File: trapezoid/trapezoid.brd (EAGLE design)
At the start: 90 x 35 mm, 29 parts, among them IC2 LGD20H, U1 MMA8452Q, U2 microSD, U3 DS3234, U4 MCP73831

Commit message: postiotedn arduino pins on board
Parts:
- moved J2 3.29 mm to (72.9, 29.9)
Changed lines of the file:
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@@
 <element name="IC2" library="microbuilder" package="L3GD20H_LGA16L" value="LGD20H" x="-49.53" y="25.4"/>
 <element name="J1" library="SparkFun-Connectors" package="1X12" value="" x="88.17" y="2.01" rot="R90"/>
-<element name="J2" library="SparkFun-Connectors" package="1X12" value="" x="76.18" y="30.45" rot="R270"/>
+<element name="J2" library="SparkFun-Connectors" package="1X12" value="" x="72.93" y="29.95" rot="R270"/>
 <element name="J3" library="SparkFun-Connectors" package="1X02_LOCK" value="" x="-49.53" y="43.18"/>
 <element name="JP1" library="SparkFun-Connectors" package="JST-2-SMD@1" value="JST" x="-43.18" y="29.21">
@@
 <wire x1="-47.31" y1="54.61" x2="-42.86" y2="54.61" width="0" layer="19" extent="1-1"/>
 <wire x1="-47.31" y1="48.26" x2="-41.26" y2="49.53" width="0" layer="19" extent="1-1"/>
-<wire x1="76.18" y1="27.91" x2="-41.26" y2="49.53" width="0" layer="19" extent="1-1"/>
+<wire x1="72.93" y1="27.41" x2="-41.26" y2="49.53" width="0" layer="19" extent="1-1"/>
 <wire x1="-13.965" y1="38.6" x2="-15.24" y2="48.2299" width="0" layer="19" extent="1-1"/>
 <wire x1="-13.965" y1="37.6" x2="-13.965" y2="38.6" width="0" layer="19" extent="1-1"/>
@@
 <contactref element="U2" pad="2"/>
 <contactref element="J2" pad="12"/>
-<wire x1="-21.81" y1="11.57" x2="76.18" y2="2.51" width="0" layer="19" extent="1-1"/>
+<wire x1="-21.81" y1="11.57" x2="72.93" y2="2.01" width="0" layer="19" extent="1-1"/>
 </signal>
 <signal name="MOSI">
@@
 <contactref element="J2" pad="11"/>
 <contactref element="U3" pad="17"/>
-<wire x1="-22.225" y1="32.625" x2="76.18" y2="5.05" width="0" layer="19" extent="1-1"/>
+<wire x1="-22.225" y1="32.625" x2="72.93" y2="4.55" width="0" layer="19" extent="1-1"/>
 <wire x1="-20.71" y1="11.97" x2="-22.225" y2="32.625" width="0" layer="19" extent="1-1"/>
 </signal>
@@
 <contactref element="U3" pad="20"/>
 <contactref element="U3" pad="18"/>
-<wire x1="-23.495" y1="32.625" x2="76.18" y2="10.13" width="0" layer="19" extent="1-1"/>
+<wire x1="-23.495" y1="32.625" x2="72.93" y2="9.63" width="0" layer="19" extent="1-1"/>
 <wire x1="-26.035" y1="32.625" x2="-23.495" y2="32.625" width="0" layer="19" extent="1-1"/>
 <wire x1="-18.51" y1="11.97" x2="-23.495" y2="32.625" width="0" layer="19" extent="1-1"/>
@@
 <contactref element="J2" pad="10"/>
 <contactref element="U3" pad="19"/>
-<wire x1="-24.765" y1="32.625" x2="76.18" y2="7.59" width="0" layer="19" extent="1-1"/>
+<wire x1="-24.765" y1="32.625" x2="72.93" y2="7.09" width="0" layer="19" extent="1-1"/>
 <wire x1="-16.31" y1="11.97" x2="-24.765" y2="32.625" width="0" layer="19" extent="1-1"/>
 </signal>
@@
 <contactref element="C8" pad="1"/>
 <wire x1="-14.29" y1="48.2299" x2="-17.46" y2="57.15" width="0" layer="19" extent="1-1"/>
-<wire x1="76.18" y1="30.45" x2="-17.46" y2="57.15" width="0" layer="19" extent="1-1"/>
-<wire x1="-42.18" y1="25.51" x2="76.18" y2="30.45" width="0" layer="19" extent="1-1"/>
+<wire x1="72.93" y1="29.95" x2="-17.46" y2="57.15" width="0" layer="19" extent="1-1"/>
+<wire x1="-42.18" y1="25.51" x2="72.93" y2="29.95" width="0" layer="19" extent="1-1"/>
 </signal>
 <signal name="N$3">
@@
 <wire x1="-42.56" y1="49.53" x2="-40.96" y2="54.61" width="0" layer="19" extent="1-1"/>
 <wire x1="-49.21" y1="48.26" x2="-42.56" y2="49.53" width="0" layer="19" extent="1-1"/>
-<wire x1="76.18" y1="22.83" x2="-42.56" y2="49.53" width="0" layer="19" extent="1-1"/>
+<wire x1="72.93" y1="22.33" x2="-42.56" y2="49.53" width="0" layer="19" extent="1-1"/>
 <wire x1="-16.515" y1="39.1" x2="-18.034" y2="49.53" width="0" layer="19" extent="1-1"/>
 <wire x1="-14.74" y1="39.375" x2="-16.515" y2="39.1" width="0" layer="19" extent="1-1"/>

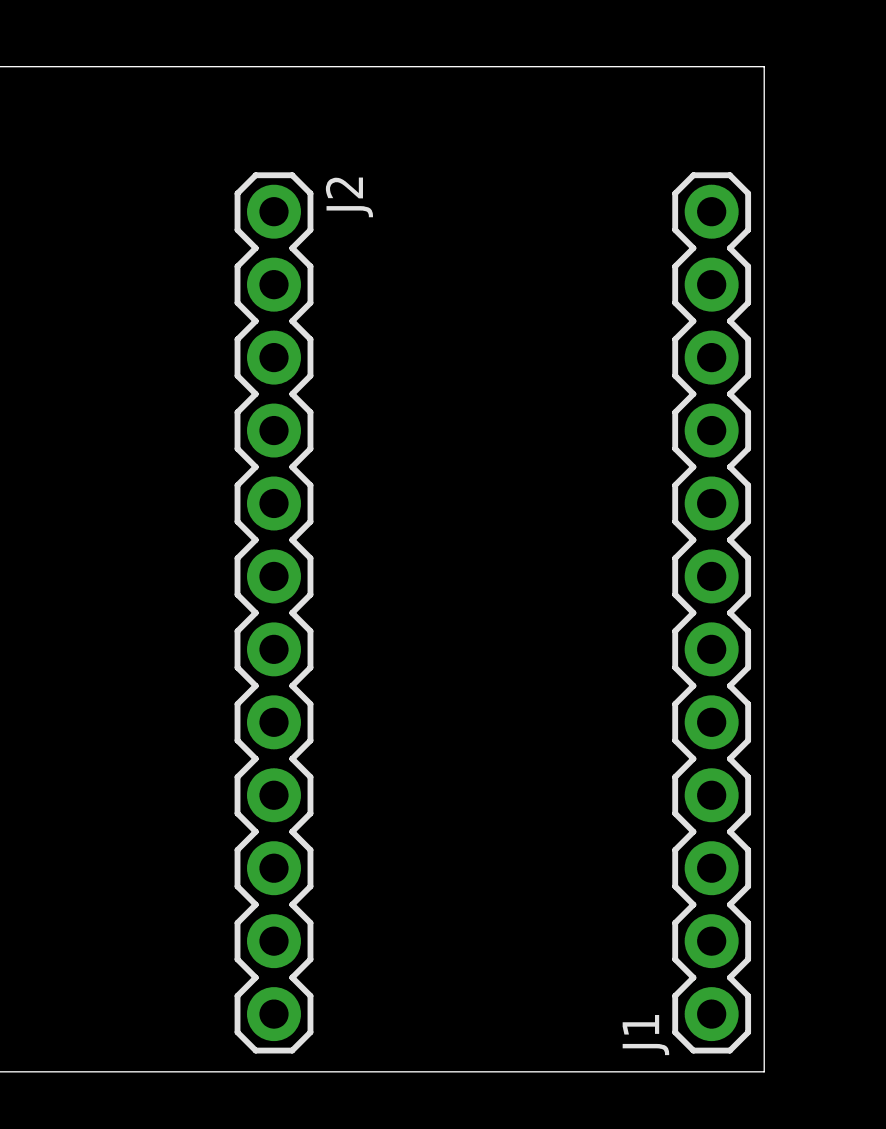
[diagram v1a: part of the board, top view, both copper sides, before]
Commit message: postiotend arduino pins on board correctly
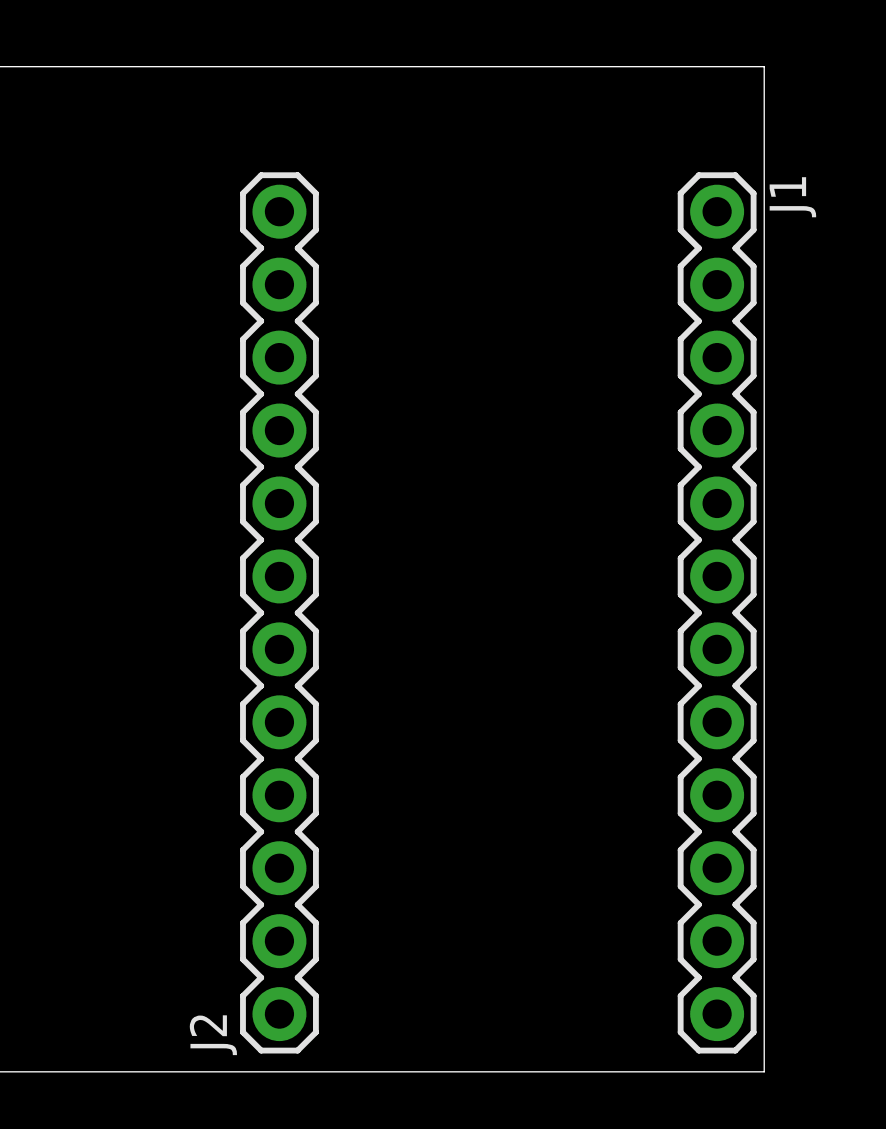
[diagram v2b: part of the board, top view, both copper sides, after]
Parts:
- moved J1 27.9 mm to (88.4, 29.9), turned to 270 degrees
- moved J2 27.9 mm to (73.1, 2.01), turned to 90 degrees
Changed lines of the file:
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@@
 </element>
 <element name="IC2" library="microbuilder" package="L3GD20H_LGA16L" value="LGD20H" x="-49.53" y="25.4"/>
-<element name="J1" library="SparkFun-Connectors" package="1X12" value="" x="88.17" y="2.01" rot="R90"/>
-<element name="J2" library="SparkFun-Connectors" package="1X12" value="" x="72.93" y="29.95" rot="R270"/>
+<element name="J1" library="SparkFun-Connectors" package="1X12" value="" x="88.36" y="29.95" rot="R270"/>
+<element name="J2" library="SparkFun-Connectors" package="1X12" value="" x="73.12" y="2.01" rot="R90"/>
 <element name="J3" library="SparkFun-Connectors" package="1X02_LOCK" value="" x="-49.53" y="43.18"/>
 <element name="JP1" library="SparkFun-Connectors" package="JST-2-SMD@1" value="JST" x="-43.18" y="29.21">
@@
 <wire x1="-47.31" y1="54.61" x2="-42.86" y2="54.61" width="0" layer="19" extent="1-1"/>
 <wire x1="-47.31" y1="48.26" x2="-41.26" y2="49.53" width="0" layer="19" extent="1-1"/>
-<wire x1="72.93" y1="27.41" x2="-41.26" y2="49.53" width="0" layer="19" extent="1-1"/>
+<wire x1="73.12" y1="4.55" x2="-41.26" y2="49.53" width="0" layer="19" extent="1-1"/>
 <wire x1="-13.965" y1="38.6" x2="-15.24" y2="48.2299" width="0" layer="19" extent="1-1"/>
 <wire x1="-13.965" y1="37.6" x2="-13.965" y2="38.6" width="0" layer="19" extent="1-1"/>
@@
 <wire x1="-18.415" y1="32.625" x2="-17.145" y2="32.625" width="0" layer="19" extent="1-1"/>
 <wire x1="-19.685" y1="32.625" x2="-18.415" y2="32.625" width="0" layer="19" extent="1-1"/>
-<wire x1="88.17" y1="22.33" x2="-19.685" y2="32.625" width="0" layer="19" extent="1-1"/>
+<wire x1="88.36" y1="9.63" x2="-19.685" y2="32.625" width="0" layer="19" extent="1-1"/>
 <wire x1="-14.605" y1="23.255" x2="-14.605" y2="32.625" width="0" layer="19" extent="1-1"/>
 <wire x1="-15.875" y1="23.255" x2="-14.605" y2="23.255" width="0" layer="19" extent="1-1"/>
@@
 <contactref element="U2" pad="2"/>
 <contactref element="J2" pad="12"/>
-<wire x1="-21.81" y1="11.57" x2="72.93" y2="2.01" width="0" layer="19" extent="1-1"/>
+<wire x1="-21.81" y1="11.57" x2="73.12" y2="29.95" width="0" layer="19" extent="1-1"/>
 </signal>
 <signal name="MOSI">
@@
 <contactref element="J2" pad="11"/>
 <contactref element="U3" pad="17"/>
-<wire x1="-22.225" y1="32.625" x2="72.93" y2="4.55" width="0" layer="19" extent="1-1"/>
+<wire x1="-22.225" y1="32.625" x2="73.12" y2="27.41" width="0" layer="19" extent="1-1"/>
 <wire x1="-20.71" y1="11.97" x2="-22.225" y2="32.625" width="0" layer="19" extent="1-1"/>
 </signal>
@@
 <contactref element="U3" pad="20"/>
 <contactref element="U3" pad="18"/>
-<wire x1="-23.495" y1="32.625" x2="72.93" y2="9.63" width="0" layer="19" extent="1-1"/>
+<wire x1="-23.495" y1="32.625" x2="73.12" y2="22.33" width="0" layer="19" extent="1-1"/>
 <wire x1="-26.035" y1="32.625" x2="-23.495" y2="32.625" width="0" layer="19" extent="1-1"/>
 <wire x1="-18.51" y1="11.97" x2="-23.495" y2="32.625" width="0" layer="19" extent="1-1"/>
@@
 <contactref element="J2" pad="10"/>
 <contactref element="U3" pad="19"/>
-<wire x1="-24.765" y1="32.625" x2="72.93" y2="7.09" width="0" layer="19" extent="1-1"/>
+<wire x1="-24.765" y1="32.625" x2="73.12" y2="24.87" width="0" layer="19" extent="1-1"/>
 <wire x1="-16.31" y1="11.97" x2="-24.765" y2="32.625" width="0" layer="19" extent="1-1"/>
 </signal>
@@
 <contactref element="J1" pad="8"/>
 <contactref element="U3" pad="5"/>
-<wire x1="-20.955" y1="23.255" x2="88.17" y2="19.79" width="0" layer="19" extent="1-1"/>
+<wire x1="-20.955" y1="23.255" x2="88.36" y2="12.17" width="0" layer="19" extent="1-1"/>
 </signal>
 <signal name="RTC_CS">
 <contactref element="J1" pad="1"/>
 <contactref element="U3" pad="1"/>
-<wire x1="-26.035" y1="23.255" x2="88.17" y2="2.01" width="0" layer="19" extent="1-1"/>
+<wire x1="-26.035" y1="23.255" x2="88.36" y2="29.95" width="0" layer="19" extent="1-1"/>
 </signal>
 <signal name="V_RAW">
@@
 <contactref element="C8" pad="1"/>
 <wire x1="-14.29" y1="48.2299" x2="-17.46" y2="57.15" width="0" layer="19" extent="1-1"/>
-<wire x1="72.93" y1="29.95" x2="-17.46" y2="57.15" width="0" layer="19" extent="1-1"/>
-<wire x1="-42.18" y1="25.51" x2="72.93" y2="29.95" width="0" layer="19" extent="1-1"/>
+<wire x1="73.12" y1="2.01" x2="-17.46" y2="57.15" width="0" layer="19" extent="1-1"/>
+<wire x1="-42.18" y1="25.51" x2="73.12" y2="2.01" width="0" layer="19" extent="1-1"/>
 </signal>
 <signal name="N$3">
@@
 <wire x1="-42.56" y1="49.53" x2="-40.96" y2="54.61" width="0" layer="19" extent="1-1"/>
 <wire x1="-49.21" y1="48.26" x2="-42.56" y2="49.53" width="0" layer="19" extent="1-1"/>
-<wire x1="72.93" y1="22.33" x2="-42.56" y2="49.53" width="0" layer="19" extent="1-1"/>
+<wire x1="73.12" y1="9.63" x2="-42.56" y2="49.53" width="0" layer="19" extent="1-1"/>
 <wire x1="-16.515" y1="39.1" x2="-18.034" y2="49.53" width="0" layer="19" extent="1-1"/>
 <wire x1="-14.74" y1="39.375" x2="-16.515" y2="39.1" width="0" layer="19" extent="1-1"/>

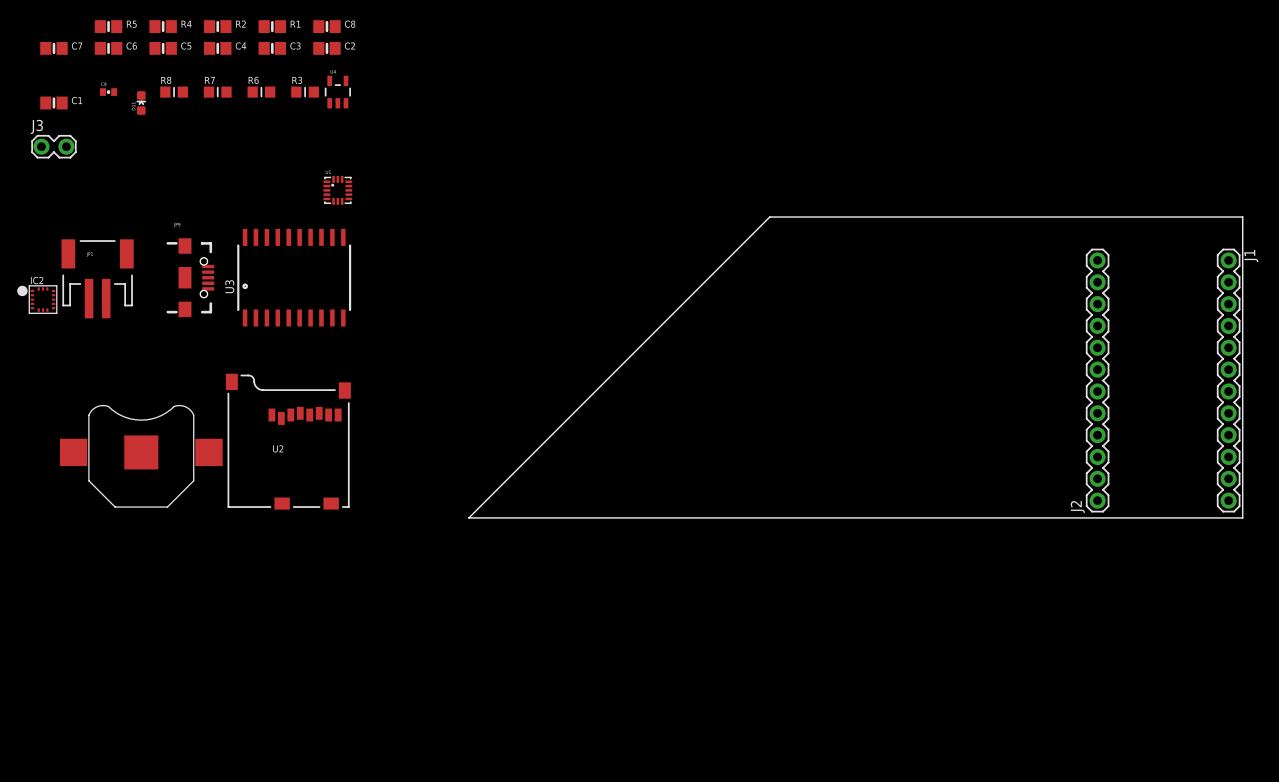
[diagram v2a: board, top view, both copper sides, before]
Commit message: possistioned i2c pins
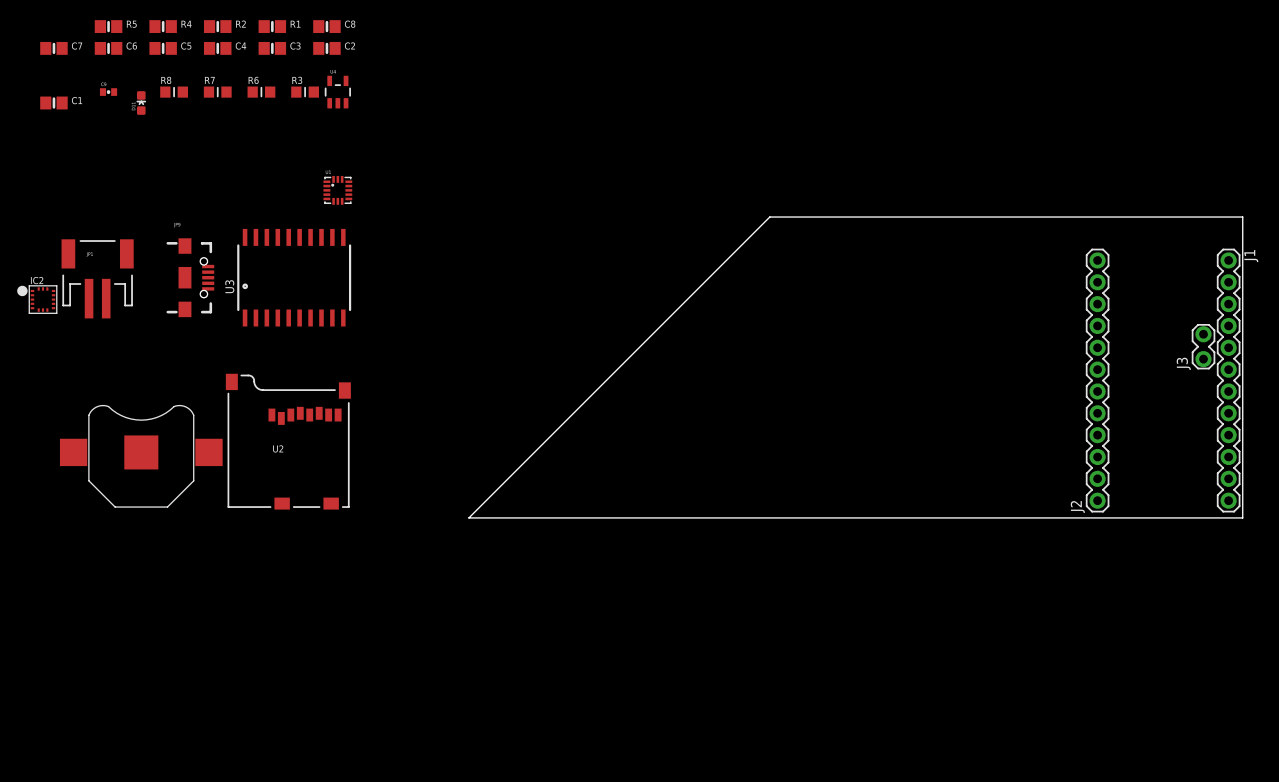
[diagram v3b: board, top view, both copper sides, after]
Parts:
- moved J3 137.2 mm to (85.4, 18.6), turned to 90 degrees
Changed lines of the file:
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@@
 <setting verticaltext="up"/>
 </settings>
-<grid distance="0.05" unitdist="inch" unit="inch" style="lines" multiple="1" display="yes" altdistance="0.025" altunitdist="inch" altunit="inch"/>
+<grid distance="0.05" unitdist="inch" unit="inch" style="lines" multiple="1" display="yes" altdistance="0.005" altunitdist="inch" altunit="inch"/>
 <layers>
 <layer number="1" name="Top" color="4" fill="1" visible="yes" active="yes"/>
@@
 <element name="J1" library="SparkFun-Connectors" package="1X12" value="" x="88.36" y="29.95" rot="R270"/>
 <element name="J2" library="SparkFun-Connectors" package="1X12" value="" x="73.12" y="2.01" rot="R90"/>
-<element name="J3" library="SparkFun-Connectors" package="1X02_LOCK" value="" x="-49.53" y="43.18"/>
+<element name="J3" library="SparkFun-Connectors" package="1X02_LOCK" value="" x="85.439" y="18.647" rot="R90"/>
 <element name="JP1" library="SparkFun-Connectors" package="JST-2-SMD@1" value="JST" x="-43.18" y="29.21">
 <attribute name="PROD_ID" value="CONN-08352" x="-43.18" y="29.21" size="1.778" layer="27" display="off"/>
@@
 <contactref element="IC2" pad="2"/>
 <wire x1="-16.515" y1="37.6" x2="-23.81" y2="57.15" width="0" layer="19" extent="1-1"/>
-<wire x1="-46.8122" y1="43.18" x2="-23.81" y2="57.15" width="0" layer="19" extent="1-1"/>
-<wire x1="-50.755" y1="25.9" x2="-46.8122" y2="43.18" width="0" layer="19" extent="1-1"/>
+<wire x1="85.439" y1="21.3648" x2="-23.81" y2="57.15" width="0" layer="19" extent="1-1"/>
+<wire x1="-50.755" y1="25.9" x2="85.439" y2="21.3648" width="0" layer="19" extent="1-1"/>
 </signal>
 <signal name="SDA">
@@
 <contactref element="IC2" pad="3"/>
 <wire x1="-15.74" y1="36.825" x2="-28.26" y2="57.15" width="0" layer="19" extent="1-1"/>
-<wire x1="-49.7078" y1="43.18" x2="-28.26" y2="57.15" width="0" layer="19" extent="1-1"/>
-<wire x1="-50.755" y1="25.4" x2="-49.7078" y2="43.18" width="0" layer="19" extent="1-1"/>
+<wire x1="85.439" y1="18.4692" x2="-28.26" y2="57.15" width="0" layer="19" extent="1-1"/>
+<wire x1="-50.755" y1="25.4" x2="85.439" y2="18.4692" width="0" layer="19" extent="1-1"/>
 </signal>
 <signal name="SA0">

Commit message: clean up
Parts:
- moved U3 85.3 mm to (62.6, 8.29)
- moved U2 84.4 mm to (69.0, 16.7)
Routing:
- net SD_CS: track 0.00 -> 19.4 mm
- net MOSI: track 0.00 -> 16.3 mm
- net SCK: track 0.00 -> 12.4 mm
- net MISO: track 0.00 -> 9.63 mm
- added copper zone on layer 1, net GND
- added copper zone on layer 16, net GND
